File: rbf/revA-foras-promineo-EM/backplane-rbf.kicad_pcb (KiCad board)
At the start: 2 copper layers, 39.7 x 15.9 mm, 3 parts, among them J300 FTS-130-01-L-SV, J301 FTS-130-01-L-SV

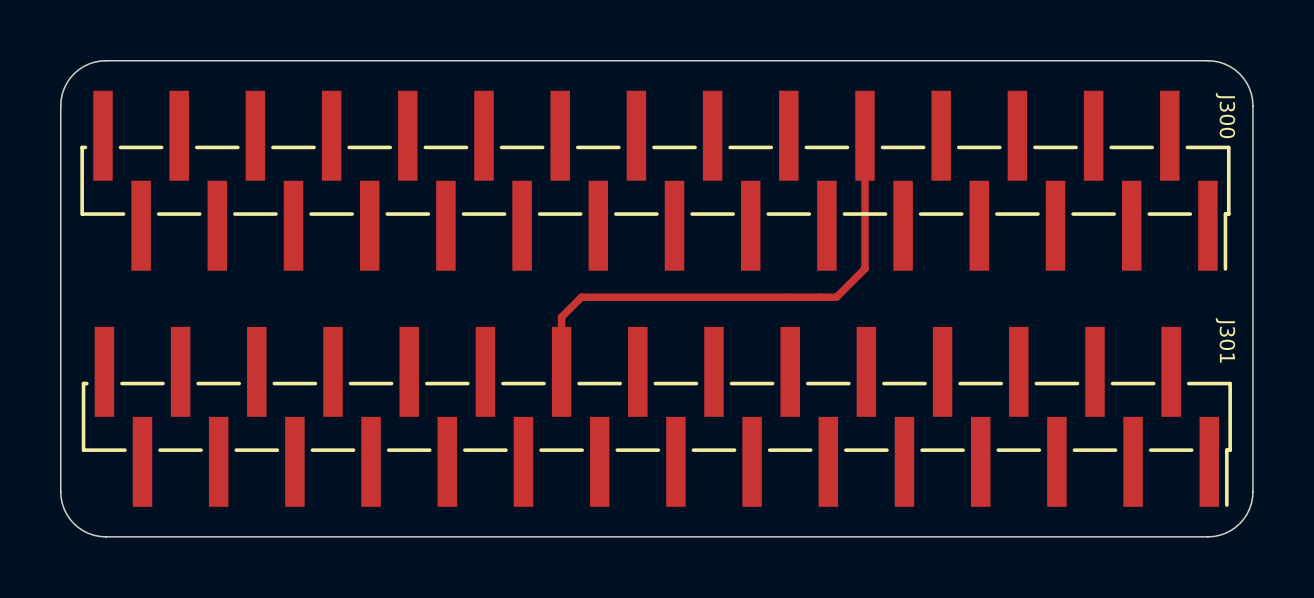
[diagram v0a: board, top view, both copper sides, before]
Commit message: updated RBF to correct pin
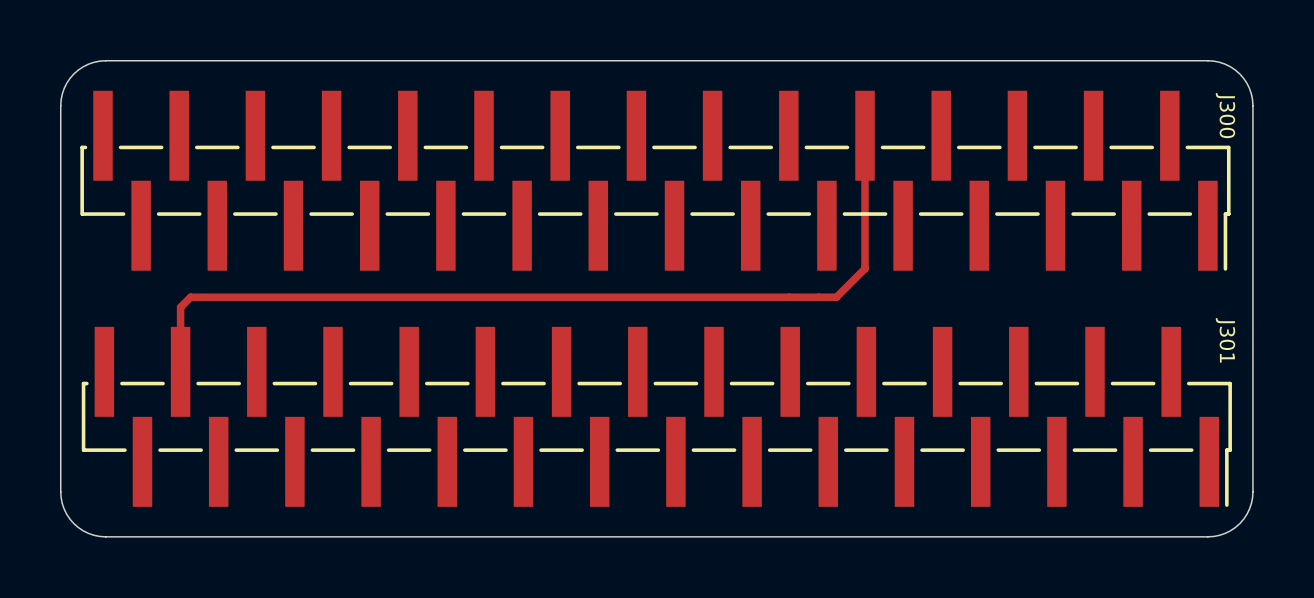
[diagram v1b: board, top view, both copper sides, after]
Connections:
- NT1 pad 2: /GND -> /H2-52
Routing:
- net /H2-52: track 0.00 -> 22.6 mm
- net /GND: track 9.68 -> 0.00 mm
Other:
- net class Default removed
